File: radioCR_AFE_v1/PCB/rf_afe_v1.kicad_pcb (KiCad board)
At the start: 2 copper layers, 125.3 x 28.9 mm, 39 parts, among them J1 Conn_Coaxial, J2 Conn_Coaxial, U1 PHA-13LN, U2 BSF108+, U3 PHA-13LN, U4 RBP188, U5 PSA8A+, U6 TCBT-6G+

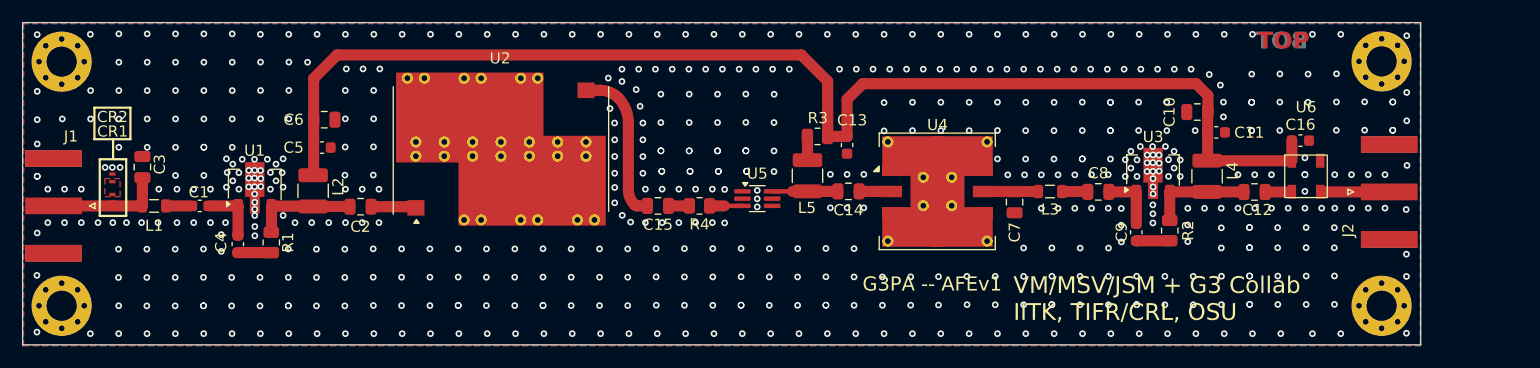
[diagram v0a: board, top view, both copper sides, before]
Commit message: attenuator added to schematic and PCB
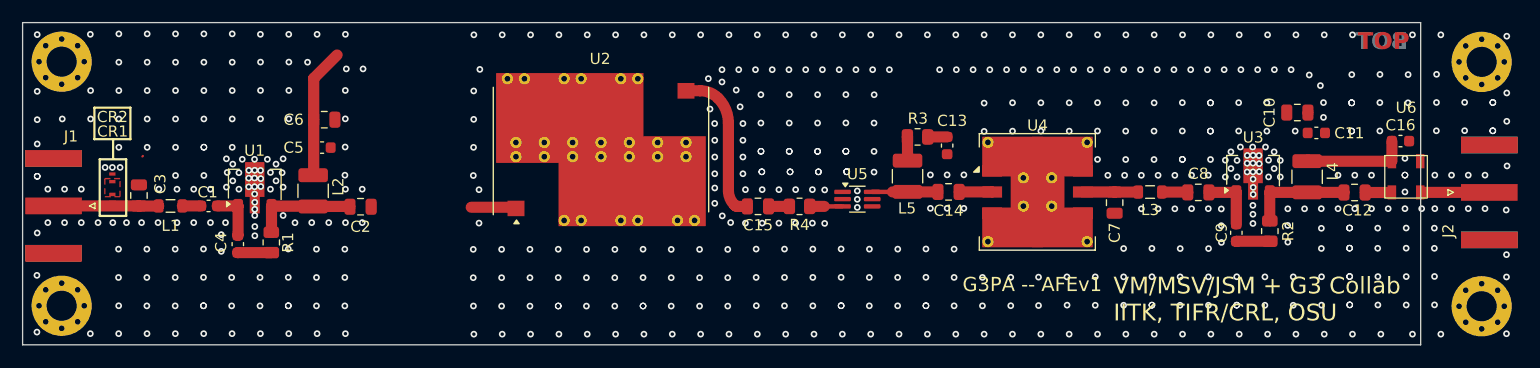
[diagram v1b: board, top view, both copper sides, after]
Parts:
- moved C11 8.97 mm to (202.7, 93.2)
- moved C13 8.97 mm to (169.6, 94.3)
- moved C14 8.97 mm to (169.7, 98.5)
- moved C15 8.97 mm to (152.6, 99.8)
- moved C16 8.97 mm to (210.2, 93.9)
- moved C9 8.97 mm to (195.5, 102.1)
- moved H5 8.97 mm to (217.5, 86.8)
- moved H6 8.97 mm to (217.5, 108.7)
- moved J2 8.97 mm to (218.2, 98.5)
- moved L3 8.97 mm to (187.8, 98.5)
- moved R2 8.97 mm to (198.5, 102.0)
- moved R3 8.97 mm to (166.9, 93.5)
- moved R4 8.97 mm to (156.3, 99.8)
- moved U3 8.97 mm to (197.0, 96.6)
- moved U4 8.97 mm to (177.7, 98.5)
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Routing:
- net +5V: track 115.1 -> 22.8 mm
- net Net-(C1-Pad2): track 5.21 -> 4.51 mm
- removed copper zone on B.Cu, net GND
- removed copper zone on F.Cu, net GND
